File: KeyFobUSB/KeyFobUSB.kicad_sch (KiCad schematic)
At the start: 44 parts, among them J1 USB_A, J3 Conn_Coaxial, SW1 SW_Push, U1 MIC5365-3.3YD5, U2 USBLC6-2SC6, U3 STM32WB55CEU6, X1 32kHz768, X2 32MHz

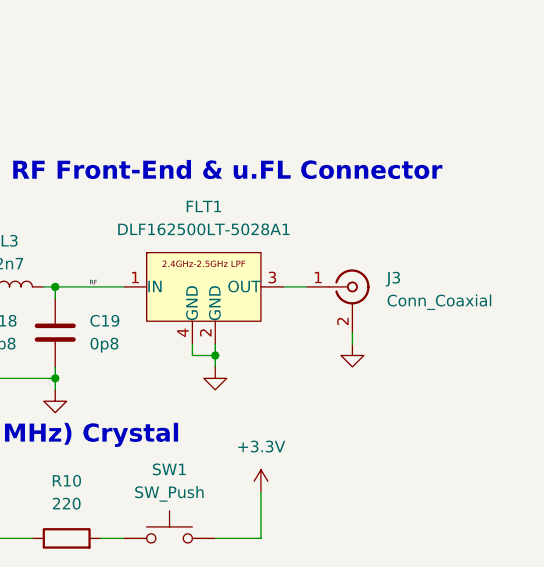
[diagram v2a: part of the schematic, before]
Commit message: Added the PCB image
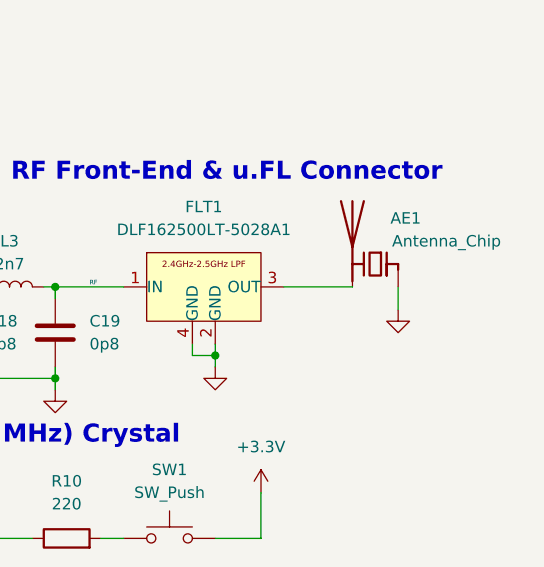
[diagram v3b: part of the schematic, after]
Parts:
- removed J3: Conn_Coaxial, Connector_Coaxial:U.FL_Hirose_U.FL-R-SMT-1_Vertical, symbol Connector:Conn_Coaxial
- added AE1: Antenna_Chip, symbol Device:Antenna_Chip
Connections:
- net GND: now also AE1.1 (FEED)
- net at FLT1.3 (OUT): now also AE1.2 (PCB_Trace)
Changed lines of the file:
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@@
 	(wire
 		(pts
-			(xy 247.65 92.71) (xy 250.19 92.71)
+			(xy 247.65 92.71) (xy 255.27 92.71)
 		)
 		(stroke
@@
 	(wire
 		(pts
-			(xy 255.27 97.79) (xy 255.27 99.06)
-		)
-		(stroke
-			(width 0)
-			(type default)
-		)
-	)
-	(wire
-		(pts
 			(xy 48.26 99.06) (xy 48.26 100.33)
 		)
@@
 	(wire
 		(pts
+			(xy 260.35 92.71) (xy 260.35 95.25)
+		)
+		(stroke
+			(width 0)
+			(type default)
+		)
+	)
+	(wire
+		(pts
 			(xy 54.61 133.35) (xy 52.07 133.35)
 		)
@@
 	)
 	(symbol
+		(lib_id "Device:Antenna_Chip")
+		(at 257.81 90.17 0)
+		(mirror y)
+		(unit 1)
+		(exclude_from_sim no)
+		(in_bom yes)
+		(on_board yes)
+		(dnp no)
+		(property "Reference" "AE1"
+			(at 262.89 85.09 0)
+			(effects
+				(font
+					(size 1.27 1.27)
+				)
+				(justify left)
+			)
+		)
+		(property "Value" "Antenna_Chip"
+			(at 271.78 87.63 0)
+			(effects
+				(font
+					(size 1.27 1.27)
+				)
+				(justify left)
+			)
+		)
+		(property "Footprint" ""
+			(at 260.35 85.725 0)
+			(effects
+				(font
+					(size 1.27 1.27)
+				)
+				(hide yes)
+			)
+		)
+		(property "Datasheet" "~"
+			(at 260.35 85.725 0)
+			(effects
+				(font
+					(size 1.27 1.27)
+				)
+				(hide yes)
+			)
+		)
+		(property "Description" "Ceramic chip antenna with pin for PCB trace"
+			(at 257.81 90.17 0)
+			(effects
+				(font
+					(size 1.27 1.27)
+				)
+				(hide yes)
+			)
+		)
+		(pin "2"
+		)
+		(pin "1"
+		)
+		(instances
+			(project ""
+				(path "/0fd3cdae-59c4-42b0-a096-27e29e27ac1f"
+					(reference "AE1")
+					(unit 1)
+				)
+			)
+		)
+	)
+	(symbol
 		(lib_id "power:GND")
 		(at 83.82 110.49 0)
@@
 	)
 	(symbol
-		(lib_id "Connector:Conn_Coaxial")
-		(at 255.27 92.71 0)
-		(unit 1)
-		(exclude_from_sim no)
-		(in_bom yes)
-		(on_board yes)
-		(dnp no)
-		(fields_autoplaced yes)
-		(property "Reference" "J3"
-			(at 259.08 91.7331 0)
-			(effects
-				(font
-					(size 1.27 1.27)
-				)
-				(justify left)
-			)
-		)
-		(property "Value" "Conn_Coaxial"
-			(at 259.08 94.2731 0)
-			(effects
-				(font
-					(size 1.27 1.27)
-				)
-				(justify left)
-			)
-		)
-		(property "Footprint" "Connector_Coaxial:U.FL_Hirose_U.FL-R-SMT-1_Vertical"
-			(at 255.27 92.71 0)
-			(effects
-				(font
-					(size 1.27 1.27)
-				)
-				(hide yes)
-			)
-		)
-		(property "Datasheet" "~"
-			(at 255.27 92.71 0)
-			(effects
-				(font
-					(size 1.27 1.27)
-				)
-				(hide yes)
-			)
-		)
-		(property "Description" "coaxial connector (BNC, SMA, SMB, SMC, Cinch/RCA, LEMO, ...)"
-			(at 255.27 92.71 0)
-			(effects
-				(font
-					(size 1.27 1.27)
-				)
-				(hide yes)
-			)
-		)
-		(property "Manufacturer " ""
-			(at 255.27 92.71 0)
-			(effects
-				(font
-					(size 1.27 1.27)
-				)
-				(hide yes)
-			)
-		)
-		(property "Manufacturer Part Number" ""
-			(at 255.27 92.71 0)
-			(effects
-				(font
-					(size 1.27 1.27)
-				)
-				(hide yes)
-			)
-		)
-		(property "distributor Link" ""
-			(at 255.27 92.71 0)
-			(effects
-				(font
-					(size 1.27 1.27)
-				)
-				(hide yes)
-			)
-		)
-		(pin "1"
-		)
-		(pin "2"
-		)
-		(instances
-			(project "KeyFobUSB"
-				(path "/0fd3cdae-59c4-42b0-a096-27e29e27ac1f"
-					(reference "J3")
-					(unit 1)
-				)
-			)
-		)
-	)
-	(symbol
 		(lib_id "Device:L")
 		(at 180.34 74.93 90)
@@
 	(symbol
 		(lib_id "power:GND")
-		(at 255.27 99.06 0)
+		(at 260.35 95.25 0)
 		(unit 1)
 		(exclude_from_sim no)
@@
 		(fields_autoplaced yes)
 		(property "Reference" "#PWR027"
-			(at 255.27 105.41 0)
+			(at 260.35 101.6 0)
 			(effects
 				(font
@@
 		)
 		(property "Value" "GND"
-			(at 255.27 104.14 0)
+			(at 260.35 100.33 0)
 			(effects
 				(font
@@
 		)
 		(property "Footprint" ""
-			(at 255.27 99.06 0)
+			(at 260.35 95.25 0)
 			(effects
 				(font
@@
 		)
 		(property "Datasheet" ""
-			(at 255.27 99.06 0)
+			(at 260.35 95.25 0)
 			(effects
 				(font
@@
 		)
 		(property "Description" "Power symbol creates a global label with name \"GND\" , ground"
-			(at 255.27 99.06 0)
+			(at 260.35 95.25 0)
 			(effects
 				(font

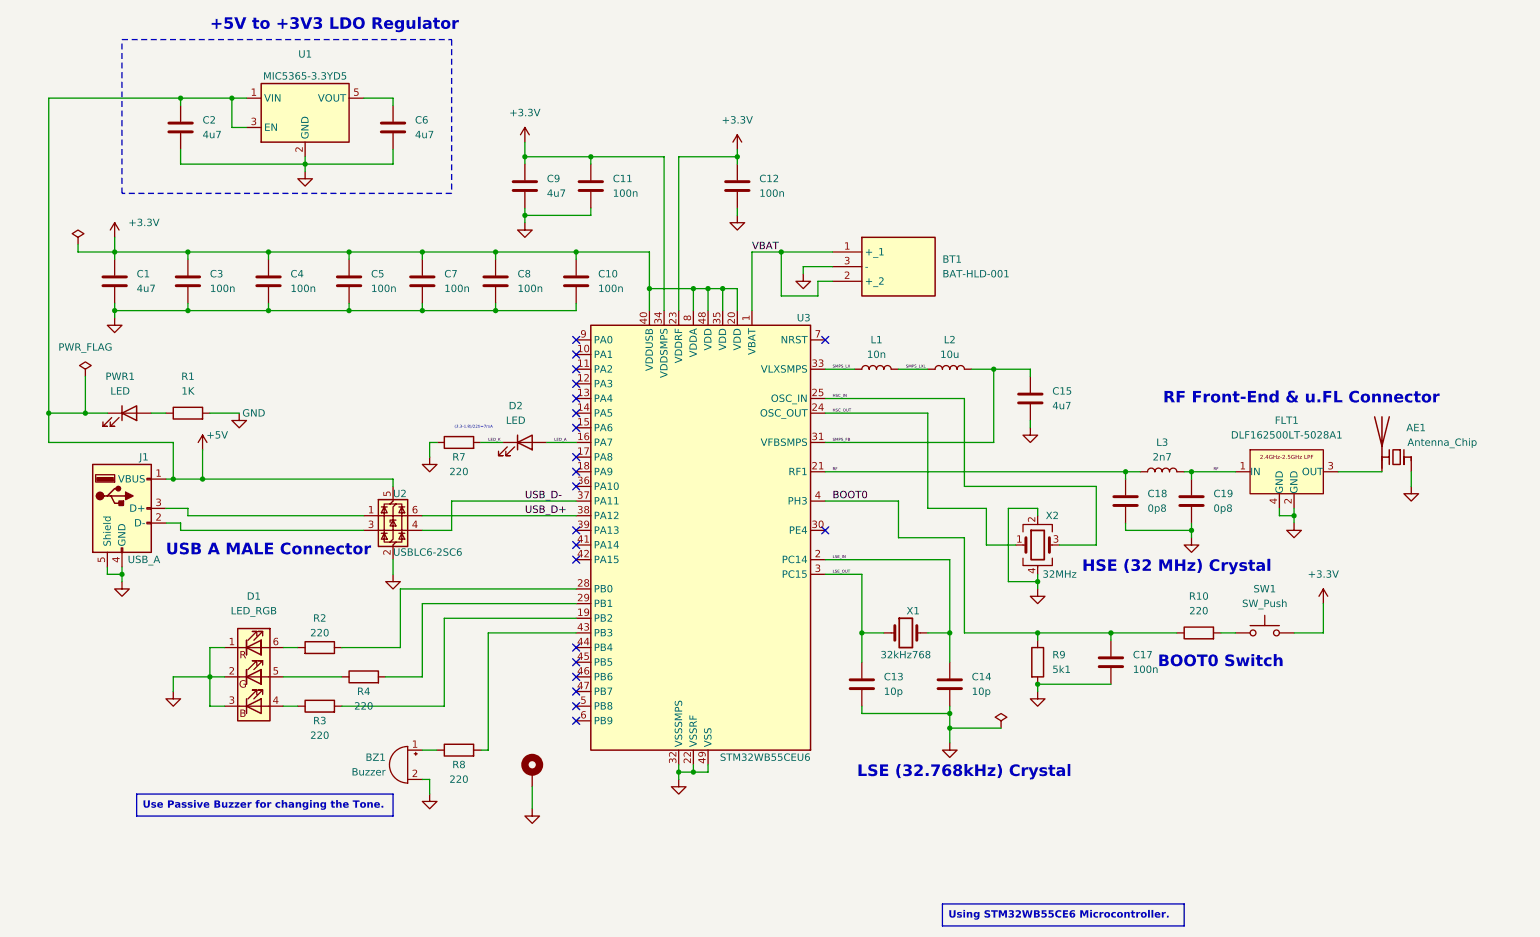
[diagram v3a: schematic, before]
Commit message: Added the Bluetooth SMD Antenna and marked the area.
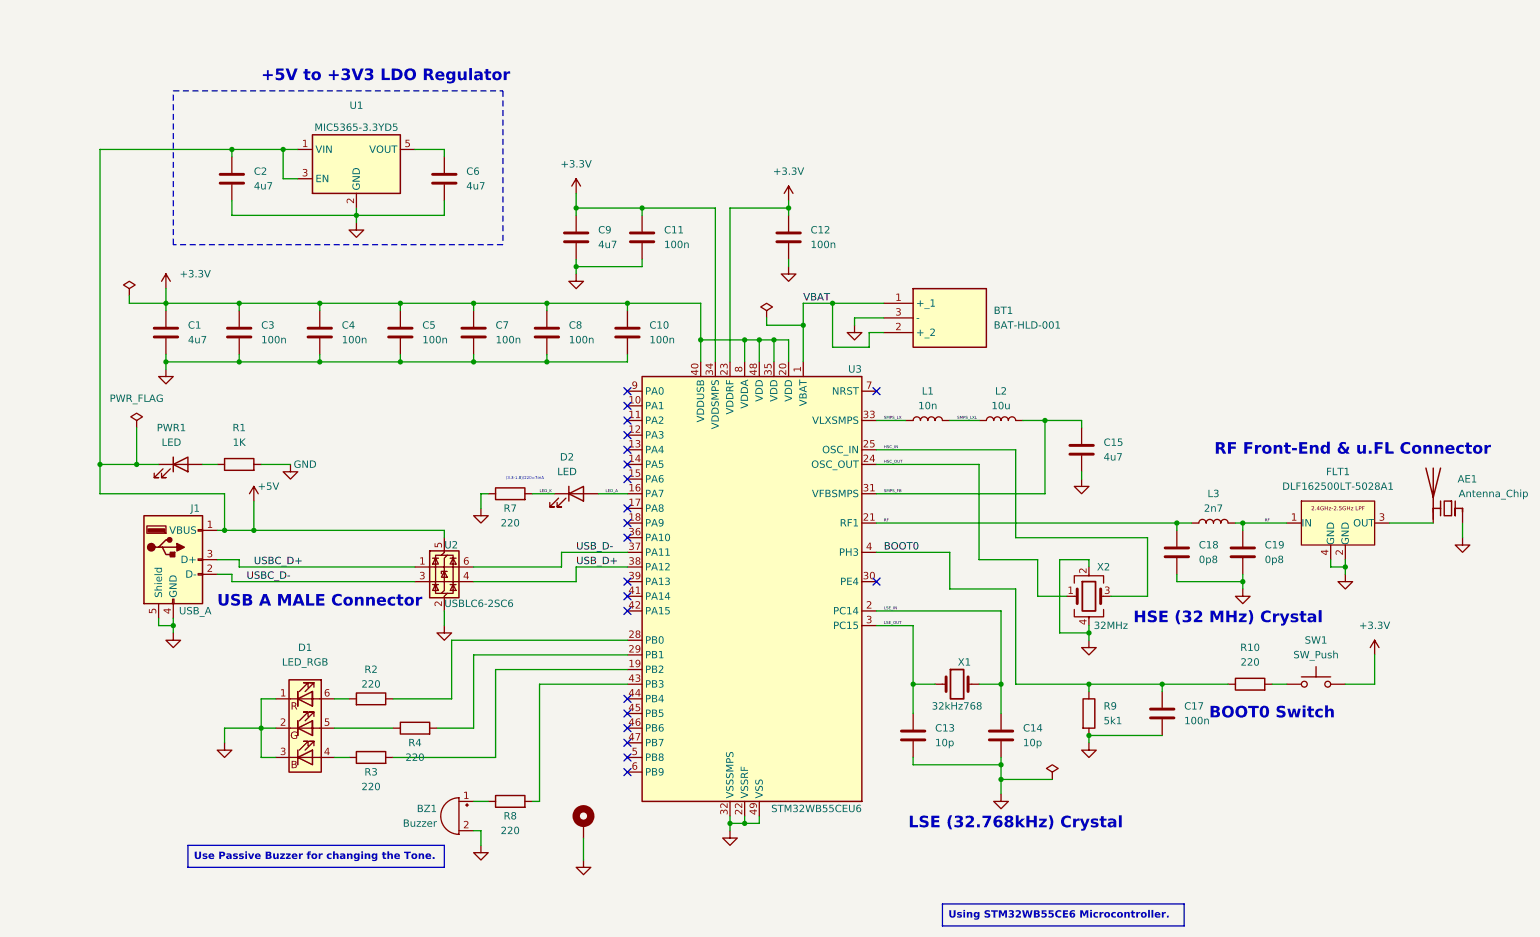
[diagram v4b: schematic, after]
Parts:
- AE1: footprint (none) -> RF Ceramic Antenna QJ-13799-2-2019:RF Ceramic Antenna QJ-13799-2-2019
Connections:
- net USB_D+: now also U2.4 (I/O2); no longer U2.6 (I/O1)
- net USB_D-: now also U2.6 (I/O1); no longer U2.4 (I/O2)
- net USBC_D-: now reaches J1.2 (D-), U2.3 (I/O2)
- net USBC_D+: now reaches J1.3 (D+), U2.1 (I/O1)
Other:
- moved on the sheet: AE1, BT1, BZ1, C1, C10, C11, C12, C13, C14, C15, C17, C18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
